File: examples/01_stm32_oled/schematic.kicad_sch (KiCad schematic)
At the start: 14 parts, among them U1 STM32F103C8Tx, U2 SSD1306

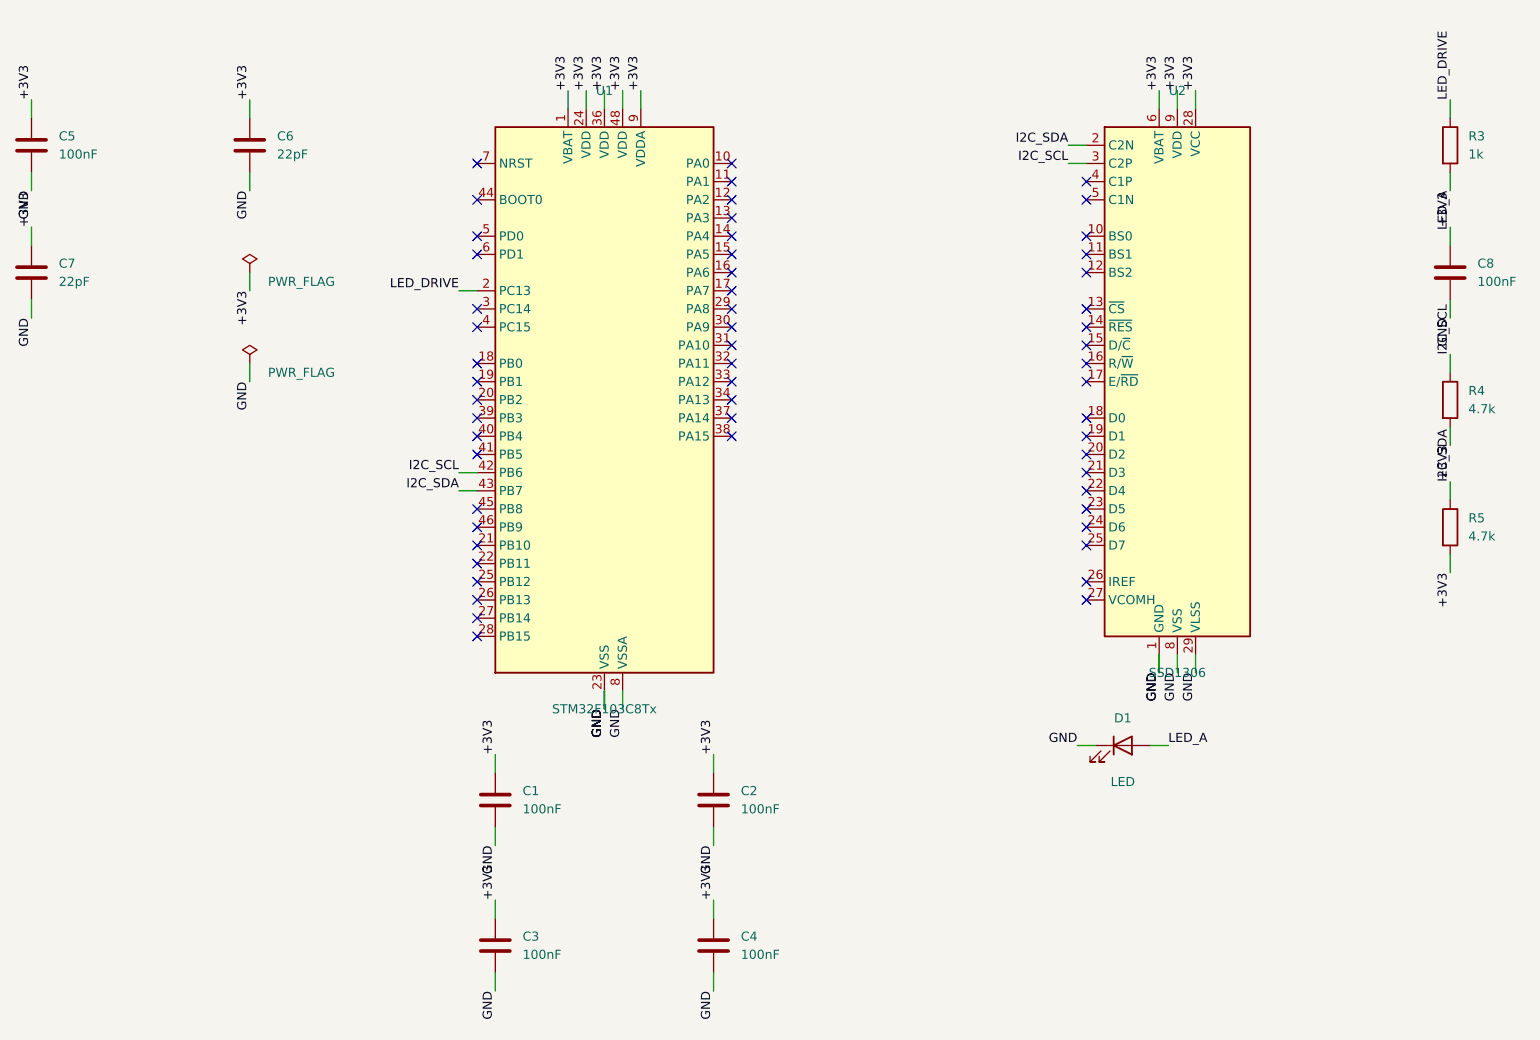
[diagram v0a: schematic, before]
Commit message: Fix OLED wiring and status LEDs; regenerate the OLED example
- A bare SSD1306 panel symbol used on I2C becomes a 4-pin OLED module header (GND, VCC, SCL, SDA);
  the model had been wiring the I2C lines to the panel's charge-pump pins
- Bus device lists follow the rename; a bus left with no devices is dropped
- A multi-colour LED picked for a plain status LED becomes Device:LED
- Decoupling counts every chip, whatever its reference name (BME280, OLED)
- Parts listed but not wired are completed or removed; a requested crystal is added; a design is not
  accepted while a resistor, capacitor or LED has an open terminal
- examples/01_stm32_oled regenerated with the fixed pipeline

Co-Authored-By: Claude Opus 5.5 <noreply@anthropic.com>
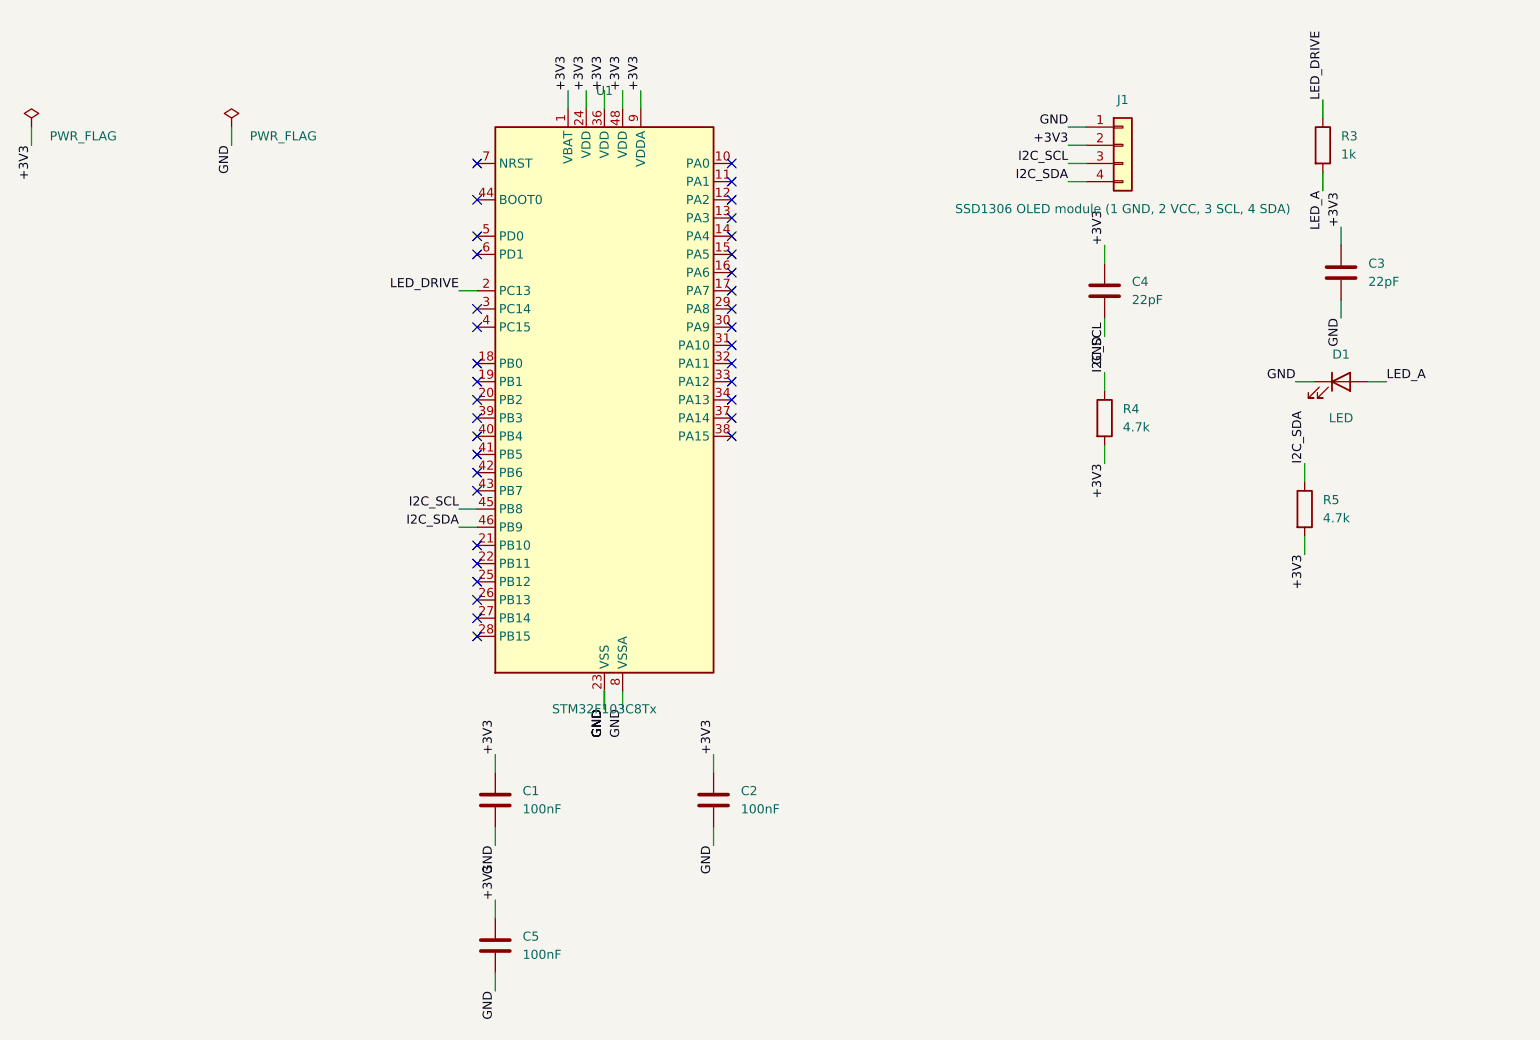
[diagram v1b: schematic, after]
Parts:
- removed C6, C7: 22pF, symbol Device:C
- removed C8: 100nF, symbol Device:C
- removed U2: SSD1306, symbol Display_Graphic:OLED-128O064D
- added J1: SSD1306 OLED module (1 GND, 2 VCC, 3 SCL, 4 SDA), symbol Connector_Generic:Conn_01x04
- C3, C4: value 100nF -> 22pF
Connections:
- net +3V3: now also J1.2 (Pin_2)
- net GND: now also J1.1 (Pin_1)
- net I2C_SCL: now also U1.45 (PB8), J1.3 (Pin_3); no longer U1.42 (PB6)
- net I2C_SDA: now also U1.46 (PB9), J1.4 (Pin_4); no longer U1.43 (PB7)
- no-connect marks 56 -> 36
